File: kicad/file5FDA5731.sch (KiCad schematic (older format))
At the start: 103 parts, among them J4 Screw_Terminal_01x02, M1 BSC014N04LSI, M11 BSC014N04LSI, M12 BSC010N04LSI, M13 BSC015NE2LS5I, M14 BSC009NE2LS5I, M15 BSC014N04LSI, M17 BSC015NE2LS5I, M2 BSC010N04LSI, M3 BSC015NE2LS5I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

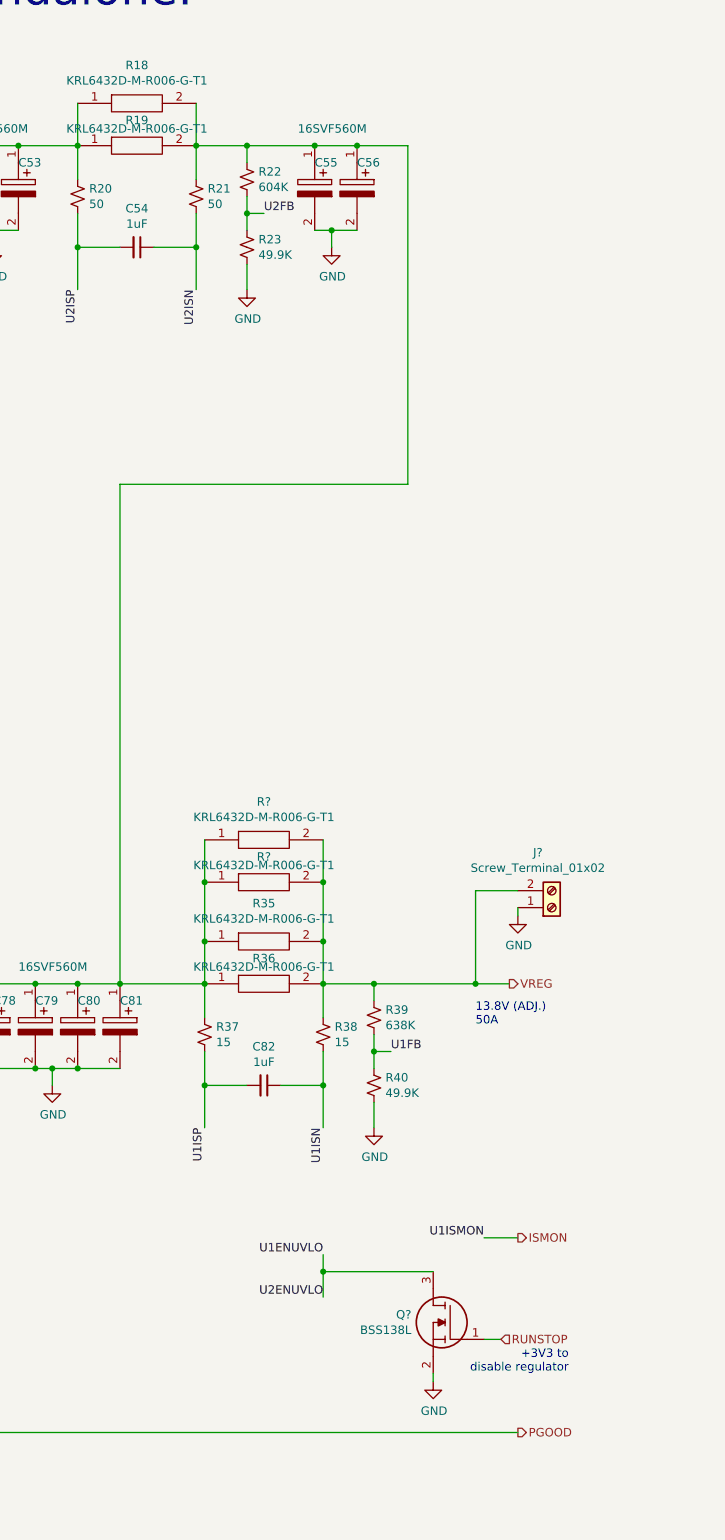
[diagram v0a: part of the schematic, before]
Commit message: Jumpers for power reg int/ext voltage control
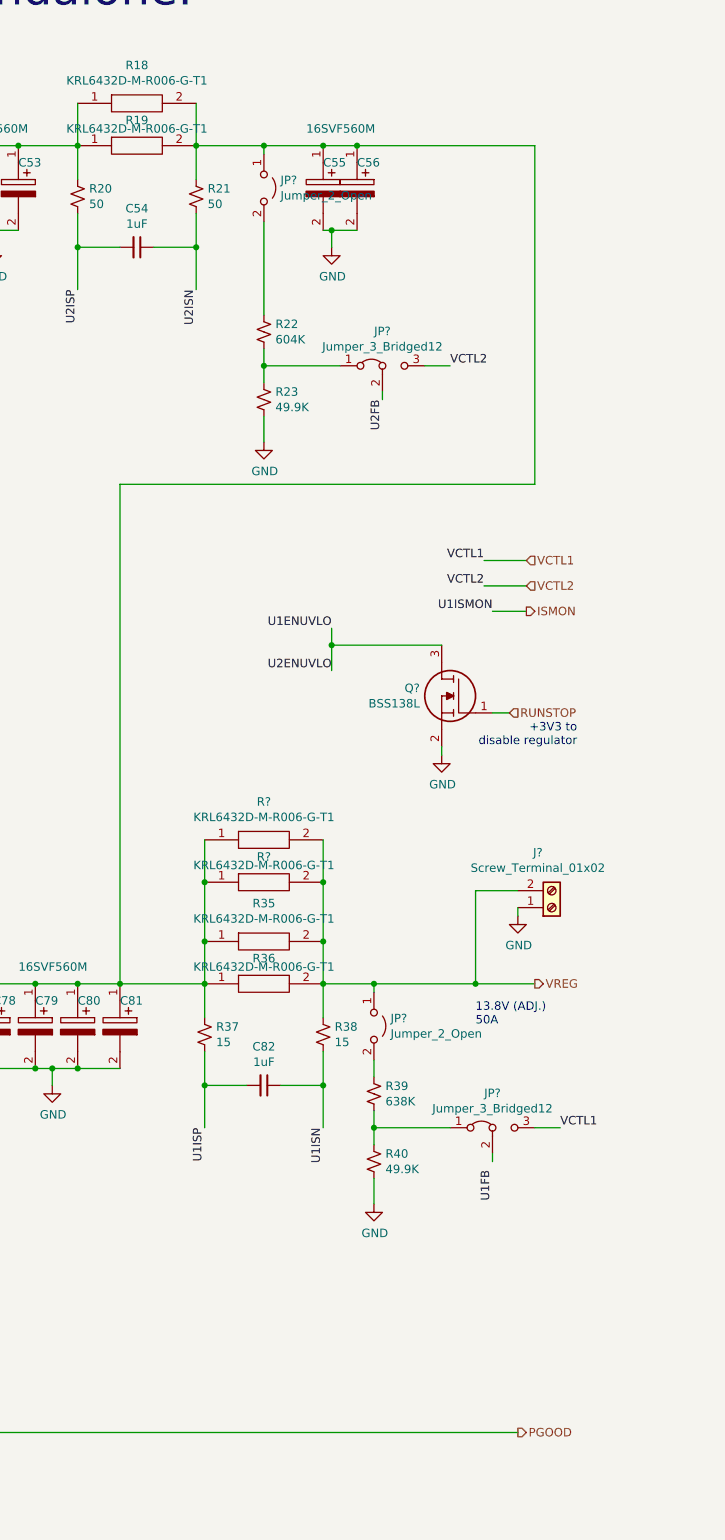
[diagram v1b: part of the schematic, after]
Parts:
- added JP? (x2): Jumper_2_Open, symbol Jumper:Jumper_2_Open
- added JP? (x2): Jumper_3_Bridged12, symbol Jumper:Jumper_3_Bridged12
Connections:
- net U1FB: no longer R39.2, R40.1
- net U1VOUT: now also JP?.1 (A); no longer R22.1
- net U2FB: now also JP?.2 (C); no longer R22.2, R23.1
- net VREG: now also JP?.1 (A); no longer R39.1
- new net: JP?.2 (B), R39.1
- new net: JP?.1 (A), R39.2, R40.1
- new net: JP?.2 (B), R22.1
- new net: JP?.1 (A), R22.2, R23.1
- new net VCTL1: JP?.3 (B)
- new net VCTL2: JP?.3 (B)
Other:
- moved on the sheet: C55, Q?, R22, R23, R39, R40

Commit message: Ethernet initial schematic; start ERC
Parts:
- gave numbers to parts that had none: 8
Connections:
- net U1FB: now also JP4.2 (C)
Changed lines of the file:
@@
 $Descr USLedger 17000 11000
 encoding utf-8
-Sheet 7 7
+Sheet 6 6
 Title "KQ9P Power Controller 12VDC"
 Date "2020-12-08"
@@
 	8800 4500 8800 4800
 Wire Wire Line
-	9400 4500 9100 4500
+	9400 4500 9300 4500
 $Comp
 L Device:R_Small_US R17
@@
 13.8V (ADJ.)\n50A
 $Comp
-L Connector:Screw_Terminal_01x02 J?
+L Connector:Screw_Terminal_01x02 J5
 U 1 1 5FE78396
 P 16150 5600
-F 0 "J?" H 16068 5275 50  0000 C CNN
+F 0 "J5" H 16068 5275 50  0000 C CNN
 F 1 "Screw_Terminal_01x02" H 16068 5366 50  0000 C CNN
 F 2 "" H 16150 5600 50  0001 C CNN
@@
 $EndComp
 $Comp
-L power:GND #PWR?
+L power:GND #PWR056
 U 1 1 5FE78DFA
 P 15950 5650
-F 0 "#PWR?" H 15950 5400 50  0001 C CNN
+F 0 "#PWR056" H 15950 5400 50  0001 C CNN
 F 1 "GND" H 15955 5477 50  0000 C CNN
 F 2 "" H 15950 5650 50  0001 C CNN
@@
 150kHz
 $Comp
-L SamacSys_Parts:BSS138L Q?
+L SamacSys_Parts:BSS138L Q1
 U 1 1 602C5287
 P 15800 4450
-F 0 "Q?" H 16229 4596 50  0000 L CNN
+F 0 "Q1" H 16229 4596 50  0000 L CNN
 F 1 "BSS138L" H 16229 4505 50  0000 L CNN
 F 2 "SOT96P237X111-3N" H 16250 4400 50  0001 L CNN
@@
 	14850 4050 14850 4200
 $Comp
-L power:GND #PWR?
+L power:GND #PWR055
 U 1 1 603D8582
 P 15500 4700
-F 0 "#PWR?" H 15500 4450 50  0001 C CNN
+F 0 "#PWR055" H 15500 4450 50  0001 C CNN
 F 1 "GND" H 15505 4527 50  0000 C CNN
 F 2 "" H 15500 4700 50  0001 C CNN
@@
 	16050 3100 13600 3100
 $Comp
-L SamacSys_Parts:KRL6432E-C-R006-F-T1 R?
+L SamacSys_Parts:KRL6432E-C-R006-F-T1 R62
 U 1 1 5FFA054E
 P 14100 5200
-F 0 "R?" H 14450 5425 50  0000 C CNN
+F 0 "R62" H 14450 5425 50  0000 C CNN
 F 1 "KRL6432D-M-R006-G-T1" H 14450 5334 50  0000 C CNN
 F 2 "RESC3163X50N" H 14650 5250 50  0001 L CNN
@@
 $EndComp
 $Comp
-L SamacSys_Parts:KRL6432E-C-R006-F-T1 R?
+L SamacSys_Parts:KRL6432E-C-R006-F-T1 R63
 U 1 1 5FFA1008
 P 14100 5450
-F 0 "R?" H 14450 5600 50  0000 C CNN
+F 0 "R63" H 14450 5600 50  0000 C CNN
 F 1 "KRL6432D-M-R006-G-T1" H 14450 5550 50  0000 C CNN
 F 2 "RESC3163X50N" H 14650 5500 50  0001 L CNN
@@
 	14050 1100 14450 1100
 $Comp
-L Jumper:Jumper_2_Open JP?
+L Jumper:Jumper_2_Open JP1
 U 1 1 5FEF3A0A
 P 14450 1350
-F 0 "JP?" V 14404 1448 50  0000 L CNN
+F 0 "JP1" V 14404 1448 50  0000 L CNN
 F 1 "Jumper_2_Open" V 14495 1448 50  0000 L CNN
 F 2 "" H 14450 1350 50  0001 C CNN
@@
 	14450 1550 14450 2100
 $Comp
-L Jumper:Jumper_3_Bridged12 JP?
+L Jumper:Jumper_3_Bridged12 JP3
 U 1 1 600DB7E1
 P 15150 2400
-F 0 "JP?" H 15150 2604 50  0000 C CNN
+F 0 "JP3" H 15150 2604 50  0000 C CNN
 F 1 "Jumper_3_Bridged12" H 15150 2513 50  0000 C CNN
 F 2 "" H 15150 2400 50  0001 C CNN
@@
 Wire Wire Line
 	15150 2550 15150 2600
-Text Label 15550 2400 0    50   ~ 0
-VCTL2
-Wire Wire Line
-	15400 2400 15550 2400
 $Comp
-L Jumper:Jumper_3_Bridged12 JP?
+L Jumper:Jumper_3_Bridged12 JP4
 U 1 1 60282FDC
 P 15800 6900
-F 0 "JP?" H 15800 7104 50  0000 C CNN
+F 0 "JP4" H 15800 7104 50  0000 C CNN
 F 1 "Jumper_3_Bridged12" H 15800 7013 50  0000 C CNN
 F 2 "" H 15800 6900 50  0001 C CNN
@@
 $EndComp
 Wire Wire Line
-	15800 7050 15800 7100
-Text Label 16200 6900 0    50   ~ 0
-VCTL1
-Wire Wire Line
-	16050 6900 16200 6900
-Wire Wire Line
 	15100 6800 15100 6900
 Wire Wire Line
@@
 Wire Wire Line
 	15100 6900 15100 7000
-Text Label 15750 3550 2    50   ~ 0
-VCTL1
-Text Label 15750 3700 2    50   ~ 0
-VCTL2
-Text HLabel 16000 3550 2    50   Input ~ 0
+Text HLabel 16050 6900 2    50   Input ~ 0
 VCTL1
-Text HLabel 16000 3700 2    50   Input ~ 0
+Text HLabel 15400 2400 2    50   Input ~ 0
 VCTL2
 Wire Wire Line
-	15750 3550 16000 3550
-Wire Wire Line
-	15750 3700 16000 3700
-Wire Wire Line
 	14800 6050 15100 6050
 $Comp
-L Jumper:Jumper_2_Open JP?
+L Jumper:Jumper_2_Open JP2
 U 1 1 6054454E
 P 15100 6300
-F 0 "JP?" V 15054 6398 50  0000 L CNN
+F 0 "JP2" V 15054 6398 50  0000 L CNN
 F 1 "Jumper_2_Open" V 15145 6398 50  0000 L CNN
 F 2 "" H 15100 6300 50  0001 C CNN
@@
 Wire Wire Line
 	15100 6500 15100 6600
+$Comp
+L power:PWR_FLAG #FLG0108
+U 1 1 600F3813
+P 9300 4500
+F 0 "#FLG0108" H 9300 4575 50  0001 C CNN
+F 1 "PWR_FLAG" H 9300 4673 50  0000 C CNN
+F 2 "" H 9300 4500 50  0001 C CNN
+F 3 "~" H 9300 4500 50  0001 C CNN
+	1    9300 4500
+	1    0    0    -1
+$EndComp
+Connection ~ 9300 4500
+Wire Wire Line
+	9300 4500 9100 4500
+Wire Wire Line
+	15800 7050 15800 7150
 $EndSCHEMATC

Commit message: Add datasheets
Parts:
- C40, C41, C42, C43, C44, C45, C46, C47, C54, C57, C66, C67, C68, C69, C70, C71, C72, C73, C82: footprint (none) -> Capacitor_SMD:C_01005_0402Metric
- C48, C49, C50, C51: footprint CAPC3216X180N -> (none)
- JP1, JP2: footprint (none) -> Connector_PinHeader_2.54mm:PinHeader_1x02_P2.54mm_Vertical
- JP3, JP4: footprint (none) -> Connector_PinHeader_2.54mm:PinHeader_1x03_P2.54mm_Vertical
- R11, R12, R15, R16, R17, R20, R21, R22, R23, R24, R25, R26, R27, R28, R29, R30, R33, R34, R37, R38, R39, R40: footprint (none) -> Resistor_SMD:R_0402_1005Metric
